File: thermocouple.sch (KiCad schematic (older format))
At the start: 11 parts, among them Q3 Q_PNP_BEC, U2 MAX31856

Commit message: updates
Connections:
- net T-: now also U2.2 (BIAS)
- net at C3.2, C4.1, R7.1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: no longer U2.2 (BIAS)
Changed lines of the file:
@@
 $Descr A4 11693 8268
 encoding utf-8
-Sheet 3 3
+Sheet 2 3
 Title ""
 Date ""
@@
 AR Path="/5B8ADEE2/5B8B5D8B" Ref="U?"  Part="1"
 AR Path="/5B8DE3E9/5B8B5D8B" Ref="U3"  Part="1"
-F 0 "U3" H 5800 4728 50  0000 C CNN
+F 0 "U2" H 5800 4728 50  0000 C CNN
 F 1 "MAX31856" H 5800 4637 50  0000 C CNN
 F 2 "Package_SO:TSSOP-14_4.4x5mm_P0.65mm" H 5950 3400 50  0001 L CNN
@@
 AR Path="/5B8ADEE2/5B8B8EAA" Ref="C?"  Part="1"
 AR Path="/5B8DE3E9/5B8B8EAA" Ref="C10"  Part="1"
-F 0 "C10" H 5515 3296 50  0000 L CNN
+F 0 "C5" H 5515 3296 50  0000 L CNN
 F 1 "0.1uF" H 5515 3205 50  0000 L CNN
 F 2 "Capacitor_SMD:C_0603_1608Metric" H 5438 3100 50  0001 C CNN
@@
 AR Path="/5B8ADEE2/5B8B8EBE" Ref="C?"  Part="1"
 AR Path="/5B8DE3E9/5B8B8EBE" Ref="C8"  Part="1"
-F 0 "C8" H 4815 4046 50  0000 L CNN
+F 0 "C3" H 4815 4046 50  0000 L CNN
 F 1 "0.1uF" H 4815 3955 50  0000 L CNN
 F 2 "Capacitor_SMD:C_0603_1608Metric" H 4738 3850 50  0001 C CNN
@@
 	4700 4150 5050 4150
 Wire Wire Line
-	5050 4150 5050 4050
-Wire Wire Line
 	5050 3950 5300 3950
 Connection ~ 4700 4150
@@
 	4700 3850 5300 3850
 Connection ~ 4700 3850
-Wire Wire Line
-	5300 4050 5050 4050
-Connection ~ 5050 4050
-Wire Wire Line
-	5050 4050 5050 3950
 $Comp
 L power:+3.3VADC #PWR0105
@@
 AR Path="/5B8ADEE2/5B8C7FF0" Ref="#PWR0114"  Part="1"
 AR Path="/5B8DE3E9/5B8C7FF0" Ref="#PWR0114"  Part="1"
-F 0 "#PWR0114" H 5700 2950 50  0001 C CNN
+F 0 "#PWR0105" H 5700 2950 50  0001 C CNN
 F 1 "+3.3VADC" H 5570 3143 50  0000 C CNN
 F 2 "" H 5550 3000 50  0001 C CNN
@@
 AR Path="/5B8ADEE2/5B8C812D" Ref="#PWR0115"  Part="1"
 AR Path="/5B8DE3E9/5B8C812D" Ref="#PWR0115"  Part="1"
-F 0 "#PWR0115" H 5250 3000 50  0001 C CNN
+F 0 "#PWR0106" H 5250 3000 50  0001 C CNN
 F 1 "GND" V 5255 3122 50  0000 R CNN
 F 2 "" H 5250 3250 50  0001 C CNN
@@
 AR Path="/5B8ADEE2/5B8C85E4" Ref="C?"  Part="1"
 AR Path="/5B8DE3E9/5B8C85E4" Ref="C11"  Part="1"
-F 0 "C11" H 6315 3296 50  0000 L CNN
+F 0 "C6" H 6315 3296 50  0000 L CNN
 F 1 "0.1uF" H 6315 3205 50  0000 L CNN
 F 2 "Capacitor_SMD:C_0603_1608Metric" H 6238 3100 50  0001 C CNN
@@
 AR Path="/5B8ADEE2/5B8C873D" Ref="#PWR0116"  Part="1"
 AR Path="/5B8DE3E9/5B8C873D" Ref="#PWR0116"  Part="1"
-F 0 "#PWR0116" H 6350 3000 50  0001 C CNN
+F 0 "#PWR0107" H 6350 3000 50  0001 C CNN
 F 1 "GND" V 6355 3122 50  0000 R CNN
 F 2 "" H 6350 3250 50  0001 C CNN
@@
 AR Path="/5B8ADEE2/5B8C8A59" Ref="#PWR0117"  Part="1"
 AR Path="/5B8DE3E9/5B8C8A59" Ref="#PWR0117"  Part="1"
-F 0 "#PWR0117" H 6050 2850 50  0001 C CNN
+F 0 "#PWR0108" H 6050 2850 50  0001 C CNN
 F 1 "+3V3" H 6065 3173 50  0000 C CNN
 F 2 "" H 6050 3000 50  0001 C CNN
@@
 AR Path="/5B8ADEE2/5B8C8C43" Ref="#PWR0118"  Part="1"
 AR Path="/5B8DE3E9/5B8C8C43" Ref="#PWR0118"  Part="1"
-F 0 "#PWR0118" H 5800 4400 50  0001 C CNN
+F 0 "#PWR0109" H 5800 4400 50  0001 C CNN
 F 1 "GND" H 5805 4477 50  0000 C CNN
 F 2 "" H 5800 4650 50  0001 C CNN
@@
 AR Path="/5B8ADEE2/5B8C91A5" Ref="#PWR0119"  Part="1"
 AR Path="/5B8DE3E9/5B8C91A5" Ref="#PWR0119"  Part="1"
-F 0 "#PWR0119" H 4700 4200 50  0001 C CNN
+F 0 "#PWR0110" H 4700 4200 50  0001 C CNN
 F 1 "GND" H 4705 4277 50  0000 C CNN
 F 2 "" H 4700 4450 50  0001 C CNN
@@
 AR Path="/5B8ADEE2/5B8C91FE" Ref="C?"  Part="1"
 AR Path="/5B8DE3E9/5B8C91FE" Ref="C7"  Part="1"
-F 0 "C7" H 4815 3746 50  0000 L CNN
+F 0 "C2" H 4815 3746 50  0000 L CNN
 F 1 "0.01uF" H 4815 3655 50  0000 L CNN
 F 2 "Capacitor_SMD:C_0603_1608Metric" H 4738 3550 50  0001 C CNN
@@
 AR Path="/5B8ADEE2/5B8C9365" Ref="#PWR0120"  Part="1"
 AR Path="/5B8DE3E9/5B8C9365" Ref="#PWR0120"  Part="1"
-F 0 "#PWR0120" H 4700 3300 50  0001 C CNN
+F 0 "#PWR0111" H 4700 3300 50  0001 C CNN
 F 1 "GND" H 4705 3377 50  0000 C CNN
 F 2 "" H 4700 3550 50  0001 C CNN
@@
 AR Path="/5B8ADEE2/5B8CA2E0" Ref="#PWR0121"  Part="1"
 AR Path="/5B8DE3E9/5B8CA2E0" Ref="#PWR0121"  Part="1"
-F 0 "#PWR0121" H 7600 3500 50  0001 C CNN
+F 0 "#PWR0112" H 7600 3500 50  0001 C CNN
 F 1 "+3V3" H 7615 3823 50  0000 C CNN
 F 2 "" H 7600 3650 50  0001 C CNN
@@
 AR Path="/5B8ADEE2/5B8CA624" Ref="D?"  Part="1"
 AR Path="/5B8DE3E9/5B8CA624" Ref="D5"  Part="1"
-F 0 "D5" H 7892 3995 50  0000 C CNN
+F 0 "D4" H 7892 3995 50  0000 C CNN
 F 1 "RED" H 7892 4086 50  0000 C CNN
 F 2 "Diode_SMD:D_0603_1608Metric" H 7900 4250 50  0001 C CNN
@@
 AR Path="/5B8ADEE2/5B8CA636" Ref="#PWR0122"  Part="1"
 AR Path="/5B8DE3E9/5B8CA636" Ref="#PWR0122"  Part="1"
-F 0 "#PWR0122" H 8100 4000 50  0001 C CNN
+F 0 "#PWR0113" H 8100 4000 50  0001 C CNN
 F 1 "GND" H 8105 4077 50  0000 C CNN
 F 2 "" H 8100 4250 50  0001 C CNN
@@
 AR Path="/5B8AB544/5BAD7E31" Ref="R6"  Part="1"
 AR Path="/5B8DE3E9/5BAD7E31" Ref="R9"  Part="1"
-F 0 "R9" V 4043 3850 50  0000 C CNN
+F 0 "R6" V 4043 3850 50  0000 C CNN
 F 1 "100" V 4134 3850 50  0000 C CNN
 F 2 "Resistor_SMD:R_0603_1608Metric" V 4180 3850 50  0001 C CNN
@@
 AR Path="/5B8AB544/5BADB677" Ref="R7"  Part="1"
 AR Path="/5B8DE3E9/5BADB677" Ref="R10"  Part="1"
-F 0 "R10" V 4043 4150 50  0000 C CNN
+F 0 "R7" V 4043 4150 50  0000 C CNN
 F 1 "100" V 4134 4150 50  0000 C CNN
 F 2 "Resistor_SMD:R_0603_1608Metric" V 4180 4150 50  0001 C CNN
@@
 AR Path="/5B8AB544/5BAE219E" Ref="R8"  Part="1"
 AR Path="/5B8DE3E9/5BAE219E" Ref="R11"  Part="1"
-F 0 "R11" V 6893 3850 50  0000 C CNN
+F 0 "R8" V 6893 3850 50  0000 C CNN
 F 1 "47k" V 6984 3850 50  0000 C CNN
 F 2 "Resistor_SMD:R_0603_1608Metric" V 7030 3850 50  0001 C CNN
@@
 T-
 Wire Wire Line
-	3950 4150 4100 4150
+	3950 4150 4050 4150
 $Comp
 L Device:C C4
@@
 AR Path="/5B8ADEE2/5BB11D31" Ref="C?"  Part="1"
 AR Path="/5B8DE3E9/5BB11D31" Ref="C9"  Part="1"
-F 0 "C9" H 4815 4346 50  0000 L CNN
+F 0 "C4" H 4815 4346 50  0000 L CNN
 F 1 "0.01uF" H 4815 4255 50  0000 L CNN
 F 2 "Capacitor_SMD:C_0603_1608Metric" H 4738 4150 50  0001 C CNN
@@
 AR Path="/5B8AB544/5BADF07C" Ref="Q3"  Part="1"
 AR Path="/5B8DE3E9/5BADF07C" Ref="Q4"  Part="1"
-F 0 "Q4" H 7691 3896 50  0000 L CNN
+F 0 "Q3" H 7691 3896 50  0000 L CNN
 F 1 "Q_PNP_BEC" H 7691 3805 50  0000 L CNN
 F 2 "Package_TO_SOT_SMD:SC-59" H 7700 3950 50  0001 C CNN
@@
 	1    0    0    1
 $EndComp
+Wire Wire Line
+	5050 3950 5050 4150
+Wire Wire Line
+	5300 4050 5150 4050
+Wire Wire Line
+	5150 4050 5150 4700
+Wire Wire Line
+	5150 4700 4050 4700
+Wire Wire Line
+	4050 4700 4050 4150
+Connection ~ 4050 4150
+Wire Wire Line
+	4050 4150 4100 4150
 $EndSCHEMATC

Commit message: update some stuff
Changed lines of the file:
@@
 $Descr A4 11693 8268
 encoding utf-8
-Sheet 2 3
+Sheet 3 3
 Title ""
 Date ""
@@
 AR Path="/5B8ADEE2/5B8B5D8B" Ref="U?"  Part="1"
 AR Path="/5B8DE3E9/5B8B5D8B" Ref="U3"  Part="1"
-F 0 "U2" H 5800 4728 50  0000 C CNN
+F 0 "U3" H 5800 4728 50  0000 C CNN
 F 1 "MAX31856" H 5800 4637 50  0000 C CNN
 F 2 "Package_SO:TSSOP-14_4.4x5mm_P0.65mm" H 5950 3400 50  0001 L CNN
@@
 AR Path="/5B8ADEE2/5B8B8EAA" Ref="C?"  Part="1"
 AR Path="/5B8DE3E9/5B8B8EAA" Ref="C10"  Part="1"
-F 0 "C5" H 5515 3296 50  0000 L CNN
+F 0 "C10" H 5515 3296 50  0000 L CNN
 F 1 "0.1uF" H 5515 3205 50  0000 L CNN
 F 2 "Capacitor_SMD:C_0603_1608Metric" H 5438 3100 50  0001 C CNN
@@
 AR Path="/5B8ADEE2/5B8B8EBE" Ref="C?"  Part="1"
 AR Path="/5B8DE3E9/5B8B8EBE" Ref="C8"  Part="1"
-F 0 "C3" H 4815 4046 50  0000 L CNN
+F 0 "C8" H 4815 4046 50  0000 L CNN
 F 1 "0.1uF" H 4815 3955 50  0000 L CNN
 F 2 "Capacitor_SMD:C_0603_1608Metric" H 4738 3850 50  0001 C CNN
@@
 AR Path="/5B8ADEE2/5B8C7FF0" Ref="#PWR0114"  Part="1"
 AR Path="/5B8DE3E9/5B8C7FF0" Ref="#PWR0114"  Part="1"
-F 0 "#PWR0105" H 5700 2950 50  0001 C CNN
+F 0 "#PWR0114" H 5700 2950 50  0001 C CNN
 F 1 "+3.3VADC" H 5570 3143 50  0000 C CNN
 F 2 "" H 5550 3000 50  0001 C CNN
@@
 AR Path="/5B8ADEE2/5B8C812D" Ref="#PWR0115"  Part="1"
 AR Path="/5B8DE3E9/5B8C812D" Ref="#PWR0115"  Part="1"
-F 0 "#PWR0106" H 5250 3000 50  0001 C CNN
+F 0 "#PWR0115" H 5250 3000 50  0001 C CNN
 F 1 "GND" V 5255 3122 50  0000 R CNN
 F 2 "" H 5250 3250 50  0001 C CNN
@@
 AR Path="/5B8ADEE2/5B8C85E4" Ref="C?"  Part="1"
 AR Path="/5B8DE3E9/5B8C85E4" Ref="C11"  Part="1"
-F 0 "C6" H 6315 3296 50  0000 L CNN
+F 0 "C11" H 6315 3296 50  0000 L CNN
 F 1 "0.1uF" H 6315 3205 50  0000 L CNN
 F 2 "Capacitor_SMD:C_0603_1608Metric" H 6238 3100 50  0001 C CNN
@@
 AR Path="/5B8ADEE2/5B8C873D" Ref="#PWR0116"  Part="1"
 AR Path="/5B8DE3E9/5B8C873D" Ref="#PWR0116"  Part="1"
-F 0 "#PWR0107" H 6350 3000 50  0001 C CNN
+F 0 "#PWR0116" H 6350 3000 50  0001 C CNN
 F 1 "GND" V 6355 3122 50  0000 R CNN
 F 2 "" H 6350 3250 50  0001 C CNN
@@
 AR Path="/5B8ADEE2/5B8C8A59" Ref="#PWR0117"  Part="1"
 AR Path="/5B8DE3E9/5B8C8A59" Ref="#PWR0117"  Part="1"
-F 0 "#PWR0108" H 6050 2850 50  0001 C CNN
+F 0 "#PWR0117" H 6050 2850 50  0001 C CNN
 F 1 "+3V3" H 6065 3173 50  0000 C CNN
 F 2 "" H 6050 3000 50  0001 C CNN
@@
 AR Path="/5B8ADEE2/5B8C8C43" Ref="#PWR0118"  Part="1"
 AR Path="/5B8DE3E9/5B8C8C43" Ref="#PWR0118"  Part="1"
-F 0 "#PWR0109" H 5800 4400 50  0001 C CNN
+F 0 "#PWR0118" H 5800 4400 50  0001 C CNN
 F 1 "GND" H 5805 4477 50  0000 C CNN
 F 2 "" H 5800 4650 50  0001 C CNN
@@
 AR Path="/5B8ADEE2/5B8C91A5" Ref="#PWR0119"  Part="1"
 AR Path="/5B8DE3E9/5B8C91A5" Ref="#PWR0119"  Part="1"
-F 0 "#PWR0110" H 4700 4200 50  0001 C CNN
+F 0 "#PWR0119" H 4700 4200 50  0001 C CNN
 F 1 "GND" H 4705 4277 50  0000 C CNN
 F 2 "" H 4700 4450 50  0001 C CNN
@@
 AR Path="/5B8ADEE2/5B8C91FE" Ref="C?"  Part="1"
 AR Path="/5B8DE3E9/5B8C91FE" Ref="C7"  Part="1"
-F 0 "C2" H 4815 3746 50  0000 L CNN
+F 0 "C7" H 4815 3746 50  0000 L CNN
 F 1 "0.01uF" H 4815 3655 50  0000 L CNN
 F 2 "Capacitor_SMD:C_0603_1608Metric" H 4738 3550 50  0001 C CNN
@@
 AR Path="/5B8ADEE2/5B8C9365" Ref="#PWR0120"  Part="1"
 AR Path="/5B8DE3E9/5B8C9365" Ref="#PWR0120"  Part="1"
-F 0 "#PWR0111" H 4700 3300 50  0001 C CNN
+F 0 "#PWR0120" H 4700 3300 50  0001 C CNN
 F 1 "GND" H 4705 3377 50  0000 C CNN
 F 2 "" H 4700 3550 50  0001 C CNN
@@
 AR Path="/5B8ADEE2/5B8CA2E0" Ref="#PWR0121"  Part="1"
 AR Path="/5B8DE3E9/5B8CA2E0" Ref="#PWR0121"  Part="1"
-F 0 "#PWR0112" H 7600 3500 50  0001 C CNN
+F 0 "#PWR0121" H 7600 3500 50  0001 C CNN
 F 1 "+3V3" H 7615 3823 50  0000 C CNN
 F 2 "" H 7600 3650 50  0001 C CNN
@@
 AR Path="/5B8ADEE2/5B8CA624" Ref="D?"  Part="1"
 AR Path="/5B8DE3E9/5B8CA624" Ref="D5"  Part="1"
-F 0 "D4" H 7892 3995 50  0000 C CNN
+F 0 "D5" H 7892 3995 50  0000 C CNN
 F 1 "RED" H 7892 4086 50  0000 C CNN
 F 2 "Diode_SMD:D_0603_1608Metric" H 7900 4250 50  0001 C CNN
@@
 AR Path="/5B8ADEE2/5B8CA636" Ref="#PWR0122"  Part="1"
 AR Path="/5B8DE3E9/5B8CA636" Ref="#PWR0122"  Part="1"
-F 0 "#PWR0113" H 8100 4000 50  0001 C CNN
+F 0 "#PWR0122" H 8100 4000 50  0001 C CNN
 F 1 "GND" H 8105 4077 50  0000 C CNN
 F 2 "" H 8100 4250 50  0001 C CNN
@@
 AR Path="/5B8AB544/5BAD7E31" Ref="R6"  Part="1"
 AR Path="/5B8DE3E9/5BAD7E31" Ref="R9"  Part="1"
-F 0 "R6" V 4043 3850 50  0000 C CNN
+F 0 "R9" V 4043 3850 50  0000 C CNN
 F 1 "100" V 4134 3850 50  0000 C CNN
 F 2 "Resistor_SMD:R_0603_1608Metric" V 4180 3850 50  0001 C CNN
@@
 AR Path="/5B8AB544/5BADB677" Ref="R7"  Part="1"
 AR Path="/5B8DE3E9/5BADB677" Ref="R10"  Part="1"
-F 0 "R7" V 4043 4150 50  0000 C CNN
+F 0 "R10" V 4043 4150 50  0000 C CNN
 F 1 "100" V 4134 4150 50  0000 C CNN
 F 2 "Resistor_SMD:R_0603_1608Metric" V 4180 4150 50  0001 C CNN
@@
 AR Path="/5B8AB544/5BAE219E" Ref="R8"  Part="1"
 AR Path="/5B8DE3E9/5BAE219E" Ref="R11"  Part="1"
-F 0 "R8" V 6893 3850 50  0000 C CNN
+F 0 "R11" V 6893 3850 50  0000 C CNN
 F 1 "47k" V 6984 3850 50  0000 C CNN
 F 2 "Resistor_SMD:R_0603_1608Metric" V 7030 3850 50  0001 C CNN
@@
 AR Path="/5B8ADEE2/5BB11D31" Ref="C?"  Part="1"
 AR Path="/5B8DE3E9/5BB11D31" Ref="C9"  Part="1"
-F 0 "C4" H 4815 4346 50  0000 L CNN
+F 0 "C9" H 4815 4346 50  0000 L CNN
 F 1 "0.01uF" H 4815 4255 50  0000 L CNN
 F 2 "Capacitor_SMD:C_0603_1608Metric" H 4738 4150 50  0001 C CNN
@@
 AR Path="/5B8AB544/5BADF07C" Ref="Q3"  Part="1"
 AR Path="/5B8DE3E9/5BADF07C" Ref="Q4"  Part="1"
-F 0 "Q3" H 7691 3896 50  0000 L CNN
+F 0 "Q4" H 7691 3896 50  0000 L CNN
 F 1 "Q_PNP_BEC" H 7691 3805 50  0000 L CNN
 F 2 "Package_TO_SOT_SMD:SC-59" H 7700 3950 50  0001 C CNN

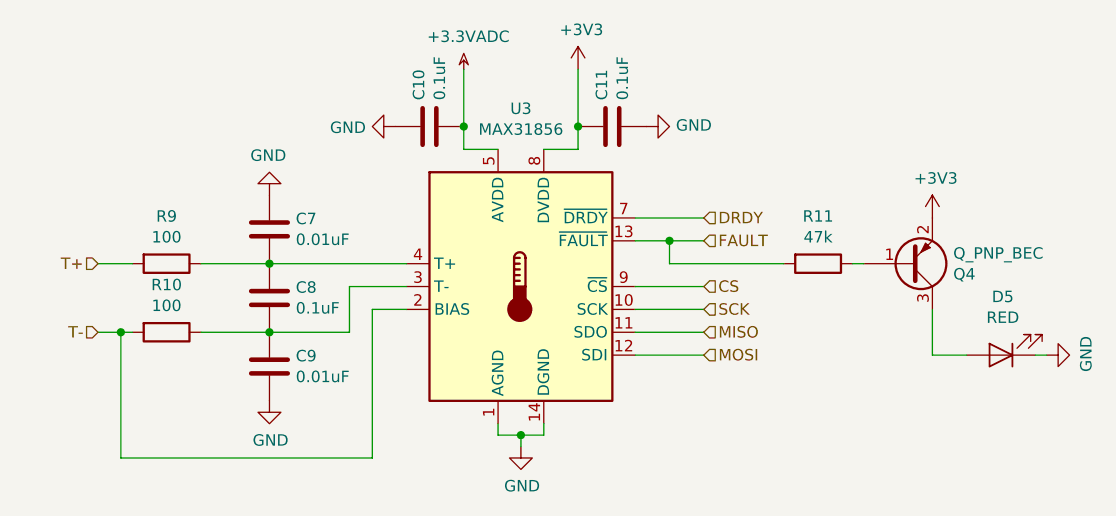
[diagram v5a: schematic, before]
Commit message: new design/ layout
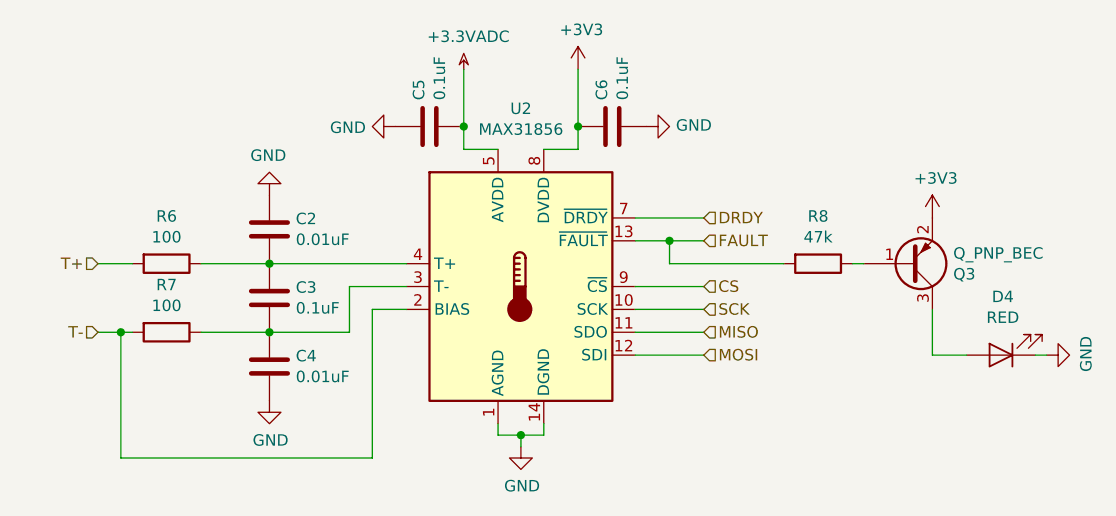
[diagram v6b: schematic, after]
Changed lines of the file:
@@
 AR Path="/5B8ADEE2/5B8B5D8B" Ref="U?"  Part="1"
 AR Path="/5B8DE3E9/5B8B5D8B" Ref="U3"  Part="1"
-F 0 "U3" H 5800 4728 50  0000 C CNN
+F 0 "U2" H 5800 4728 50  0000 C CNN
 F 1 "MAX31856" H 5800 4637 50  0000 C CNN
 F 2 "Package_SO:TSSOP-14_4.4x5mm_P0.65mm" H 5950 3400 50  0001 L CNN
@@
 AR Path="/5B8ADEE2/5B8B8EAA" Ref="C?"  Part="1"
 AR Path="/5B8DE3E9/5B8B8EAA" Ref="C10"  Part="1"
-F 0 "C10" H 5515 3296 50  0000 L CNN
+F 0 "C5" H 5515 3296 50  0000 L CNN
 F 1 "0.1uF" H 5515 3205 50  0000 L CNN
 F 2 "Capacitor_SMD:C_0603_1608Metric" H 5438 3100 50  0001 C CNN
@@
 AR Path="/5B8ADEE2/5B8B8EBE" Ref="C?"  Part="1"
 AR Path="/5B8DE3E9/5B8B8EBE" Ref="C8"  Part="1"
-F 0 "C8" H 4815 4046 50  0000 L CNN
+F 0 "C3" H 4815 4046 50  0000 L CNN
 F 1 "0.1uF" H 4815 3955 50  0000 L CNN
 F 2 "Capacitor_SMD:C_0603_1608Metric" H 4738 3850 50  0001 C CNN
@@
 AR Path="/5B8ADEE2/5B8C7FF0" Ref="#PWR0114"  Part="1"
 AR Path="/5B8DE3E9/5B8C7FF0" Ref="#PWR0114"  Part="1"
-F 0 "#PWR0114" H 5700 2950 50  0001 C CNN
+F 0 "#PWR0105" H 5700 2950 50  0001 C CNN
 F 1 "+3.3VADC" H 5570 3143 50  0000 C CNN
 F 2 "" H 5550 3000 50  0001 C CNN
@@
 AR Path="/5B8ADEE2/5B8C812D" Ref="#PWR0115"  Part="1"
 AR Path="/5B8DE3E9/5B8C812D" Ref="#PWR0115"  Part="1"
-F 0 "#PWR0115" H 5250 3000 50  0001 C CNN
+F 0 "#PWR0106" H 5250 3000 50  0001 C CNN
 F 1 "GND" V 5255 3122 50  0000 R CNN
 F 2 "" H 5250 3250 50  0001 C CNN
@@
 AR Path="/5B8ADEE2/5B8C85E4" Ref="C?"  Part="1"
 AR Path="/5B8DE3E9/5B8C85E4" Ref="C11"  Part="1"
-F 0 "C11" H 6315 3296 50  0000 L CNN
+F 0 "C6" H 6315 3296 50  0000 L CNN
 F 1 "0.1uF" H 6315 3205 50  0000 L CNN
 F 2 "Capacitor_SMD:C_0603_1608Metric" H 6238 3100 50  0001 C CNN
@@
 AR Path="/5B8ADEE2/5B8C873D" Ref="#PWR0116"  Part="1"
 AR Path="/5B8DE3E9/5B8C873D" Ref="#PWR0116"  Part="1"
-F 0 "#PWR0116" H 6350 3000 50  0001 C CNN
+F 0 "#PWR0107" H 6350 3000 50  0001 C CNN
 F 1 "GND" V 6355 3122 50  0000 R CNN
 F 2 "" H 6350 3250 50  0001 C CNN
@@
 AR Path="/5B8ADEE2/5B8C8A59" Ref="#PWR0117"  Part="1"
 AR Path="/5B8DE3E9/5B8C8A59" Ref="#PWR0117"  Part="1"
-F 0 "#PWR0117" H 6050 2850 50  0001 C CNN
+F 0 "#PWR0108" H 6050 2850 50  0001 C CNN
 F 1 "+3V3" H 6065 3173 50  0000 C CNN
 F 2 "" H 6050 3000 50  0001 C CNN
@@
 AR Path="/5B8ADEE2/5B8C8C43" Ref="#PWR0118"  Part="1"
 AR Path="/5B8DE3E9/5B8C8C43" Ref="#PWR0118"  Part="1"
-F 0 "#PWR0118" H 5800 4400 50  0001 C CNN
+F 0 "#PWR0109" H 5800 4400 50  0001 C CNN
 F 1 "GND" H 5805 4477 50  0000 C CNN
 F 2 "" H 5800 4650 50  0001 C CNN
@@
 AR Path="/5B8ADEE2/5B8C91A5" Ref="#PWR0119"  Part="1"
 AR Path="/5B8DE3E9/5B8C91A5" Ref="#PWR0119"  Part="1"
-F 0 "#PWR0119" H 4700 4200 50  0001 C CNN
+F 0 "#PWR0110" H 4700 4200 50  0001 C CNN
 F 1 "GND" H 4705 4277 50  0000 C CNN
 F 2 "" H 4700 4450 50  0001 C CNN
@@
 AR Path="/5B8ADEE2/5B8C91FE" Ref="C?"  Part="1"
 AR Path="/5B8DE3E9/5B8C91FE" Ref="C7"  Part="1"
-F 0 "C7" H 4815 3746 50  0000 L CNN
+F 0 "C2" H 4815 3746 50  0000 L CNN
 F 1 "0.01uF" H 4815 3655 50  0000 L CNN
 F 2 "Capacitor_SMD:C_0603_1608Metric" H 4738 3550 50  0001 C CNN
@@
 AR Path="/5B8ADEE2/5B8C9365" Ref="#PWR0120"  Part="1"
 AR Path="/5B8DE3E9/5B8C9365" Ref="#PWR0120"  Part="1"
-F 0 "#PWR0120" H 4700 3300 50  0001 C CNN
+F 0 "#PWR0111" H 4700 3300 50  0001 C CNN
 F 1 "GND" H 4705 3377 50  0000 C CNN
 F 2 "" H 4700 3550 50  0001 C CNN
@@
 AR Path="/5B8ADEE2/5B8CA2E0" Ref="#PWR0121"  Part="1"
 AR Path="/5B8DE3E9/5B8CA2E0" Ref="#PWR0121"  Part="1"
-F 0 "#PWR0121" H 7600 3500 50  0001 C CNN
+F 0 "#PWR0112" H 7600 3500 50  0001 C CNN
 F 1 "+3V3" H 7615 3823 50  0000 C CNN
 F 2 "" H 7600 3650 50  0001 C CNN
@@
 AR Path="/5B8ADEE2/5B8CA624" Ref="D?"  Part="1"
 AR Path="/5B8DE3E9/5B8CA624" Ref="D5"  Part="1"
-F 0 "D5" H 7892 3995 50  0000 C CNN
+F 0 "D4" H 7892 3995 50  0000 C CNN
 F 1 "RED" H 7892 4086 50  0000 C CNN
 F 2 "Diode_SMD:D_0603_1608Metric" H 7900 4250 50  0001 C CNN
@@
 AR Path="/5B8ADEE2/5B8CA636" Ref="#PWR0122"  Part="1"
 AR Path="/5B8DE3E9/5B8CA636" Ref="#PWR0122"  Part="1"
-F 0 "#PWR0122" H 8100 4000 50  0001 C CNN
+F 0 "#PWR0113" H 8100 4000 50  0001 C CNN
 F 1 "GND" H 8105 4077 50  0000 C CNN
 F 2 "" H 8100 4250 50  0001 C CNN
@@
 AR Path="/5B8AB544/5BAD7E31" Ref="R6"  Part="1"
 AR Path="/5B8DE3E9/5BAD7E31" Ref="R9"  Part="1"
-F 0 "R9" V 4043 3850 50  0000 C CNN
+F 0 "R6" V 4043 3850 50  0000 C CNN
 F 1 "100" V 4134 3850 50  0000 C CNN
 F 2 "Resistor_SMD:R_0603_1608Metric" V 4180 3850 50  0001 C CNN
@@
 AR Path="/5B8AB544/5BADB677" Ref="R7"  Part="1"
 AR Path="/5B8DE3E9/5BADB677" Ref="R10"  Part="1"
-F 0 "R10" V 4043 4150 50  0000 C CNN
+F 0 "R7" V 4043 4150 50  0000 C CNN
 F 1 "100" V 4134 4150 50  0000 C CNN
 F 2 "Resistor_SMD:R_0603_1608Metric" V 4180 4150 50  0001 C CNN
@@
 AR Path="/5B8AB544/5BAE219E" Ref="R8"  Part="1"
 AR Path="/5B8DE3E9/5BAE219E" Ref="R11"  Part="1"
-F 0 "R11" V 6893 3850 50  0000 C CNN
+F 0 "R8" V 6893 3850 50  0000 C CNN
 F 1 "47k" V 6984 3850 50  0000 C CNN
 F 2 "Resistor_SMD:R_0603_1608Metric" V 7030 3850 50  0001 C CNN
@@
 AR Path="/5B8ADEE2/5BB11D31" Ref="C?"  Part="1"
 AR Path="/5B8DE3E9/5BB11D31" Ref="C9"  Part="1"
-F 0 "C9" H 4815 4346 50  0000 L CNN
+F 0 "C4" H 4815 4346 50  0000 L CNN
 F 1 "0.01uF" H 4815 4255 50  0000 L CNN
 F 2 "Capacitor_SMD:C_0603_1608Metric" H 4738 4150 50  0001 C CNN
@@
 AR Path="/5B8AB544/5BADF07C" Ref="Q3"  Part="1"
 AR Path="/5B8DE3E9/5BADF07C" Ref="Q4"  Part="1"
-F 0 "Q4" H 7691 3896 50  0000 L CNN
+F 0 "Q3" H 7691 3896 50  0000 L CNN
 F 1 "Q_PNP_BEC" H 7691 3805 50  0000 L CNN
 F 2 "Package_TO_SOT_SMD:SC-59" H 7700 3950 50  0001 C CNN
